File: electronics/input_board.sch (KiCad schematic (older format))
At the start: 20 parts, among them IC1 ACS713, P1 CONN_01X02, P2 CONN_02X05, P3 CONN_01X02, Q1 Q_NMOS_SGD, T1 12A

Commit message: input board -> mosfet in place of triak
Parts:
- removed T1: 12A, cyplo's:sot428, symbol THYRISTOR
- added Q?: Q_NMOS_GDSD, symbol Q_NMOS_GDSD
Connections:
- wire segments 65 -> 67
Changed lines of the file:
@@
-$EndComp
-$Comp
-L THYRISTOR T1
-U 1 1 55E0D9F8
-P 6500 2000
-F 0 "T1" V 6500 2100 50  0000 C CNN
-F 1 "12A" V 6500 1850 50  0000 C CNN
-F 2 "cyplo's:sot428" H 6500 2000 60  0001 C CNN
-F 3 "http://www.nxp.com/documents/data_sheet/BT151S_SER_L_R.pdf" H 6500 2000 60  0001 C CNN
-	1    6500 2000
-	0    -1   -1   0
 $EndComp
 $Comp
@@
 	3550 1050 3800 1050
 Wire Wire Line
-	6100 2100 6100 2300
+	6100 2000 6100 2300
 Connection ~ 6100 2100
 Wire Wire Line
@@
 Wire Wire Line
 	2850 1700 2950 1700
-Wire Wire Line
-	6500 2650 6500 2200
-Wire Wire Line
-	5750 2100 6400 2100
-Wire Wire Line
-	6500 1800 6500 1300
 $Comp
 L D_Schottky D2
@@
 Wire Wire Line
 	3350 3900 3350 3800
+Wire Wire Line
+	6200 2000 6100 2000
+Wire Wire Line
+	6100 2100 5750 2100
+Wire Wire Line
+	6500 1800 6500 1300
+Wire Wire Line
+	6500 2200 6500 2650
+$Comp
+L Q_NMOS_GDSD Q?
+U 1 1 5635FEA9
+P 6400 2000
+F 0 "Q?" H 6700 2050 50  0000 R CNN
+F 1 "Q_NMOS_GDSD" H 7100 1950 50  0000 R CNN
+F 2 "" H 6600 2100 29  0000 C CNN
+F 3 "" H 6400 2000 60  0000 C CNN
+	1    6400 2000
+	1    0    0    -1
+$EndComp
+Wire Wire Line
+	6600 1800 6500 1800
+Connection ~ 6500 1800
 $EndSCHEMATC

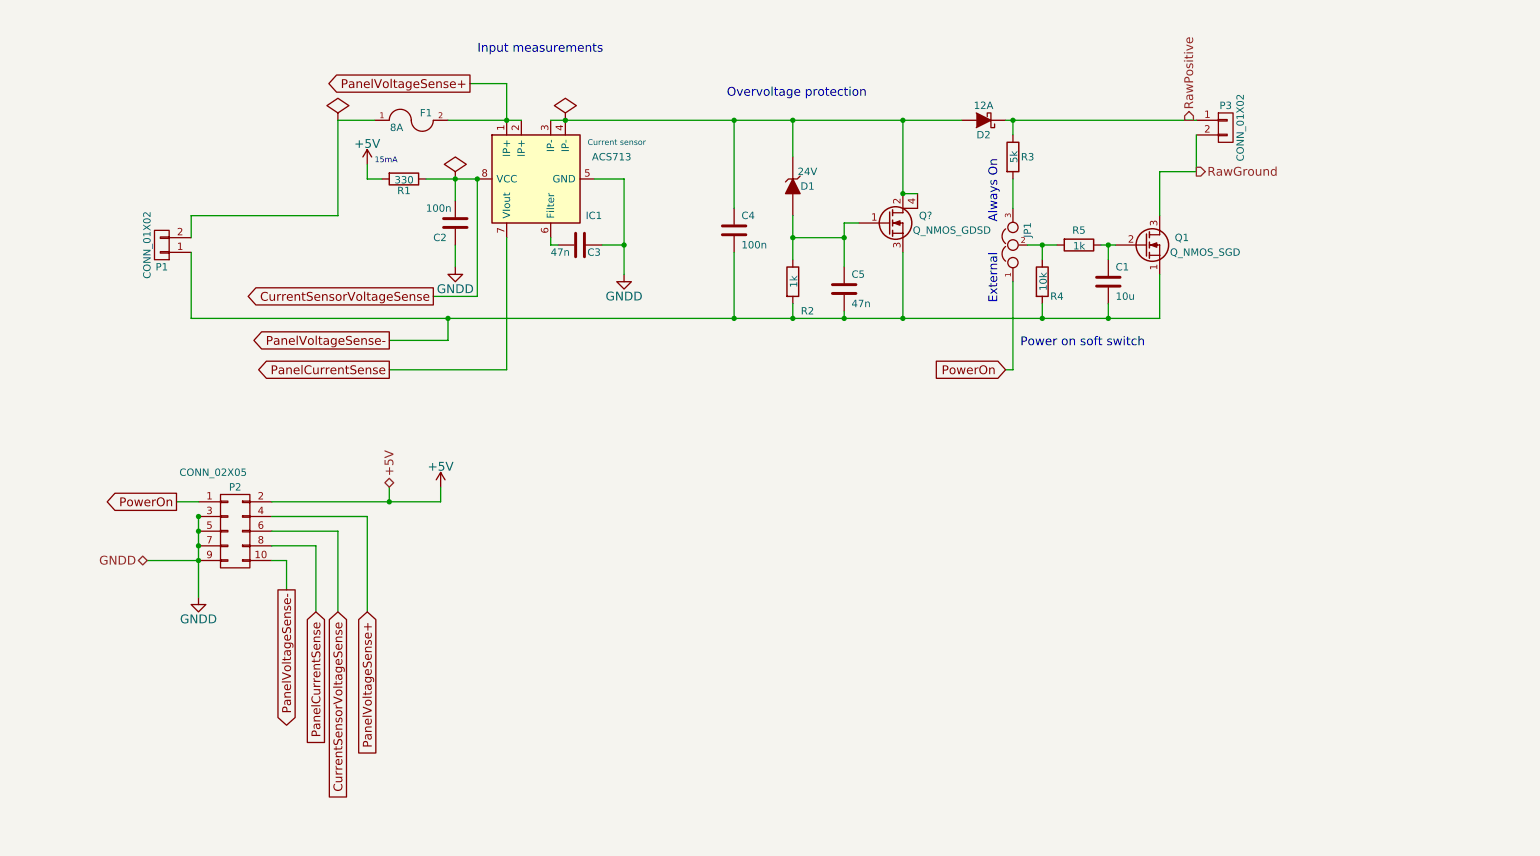
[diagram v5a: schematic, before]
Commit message: input protection: crowbar + power on switch
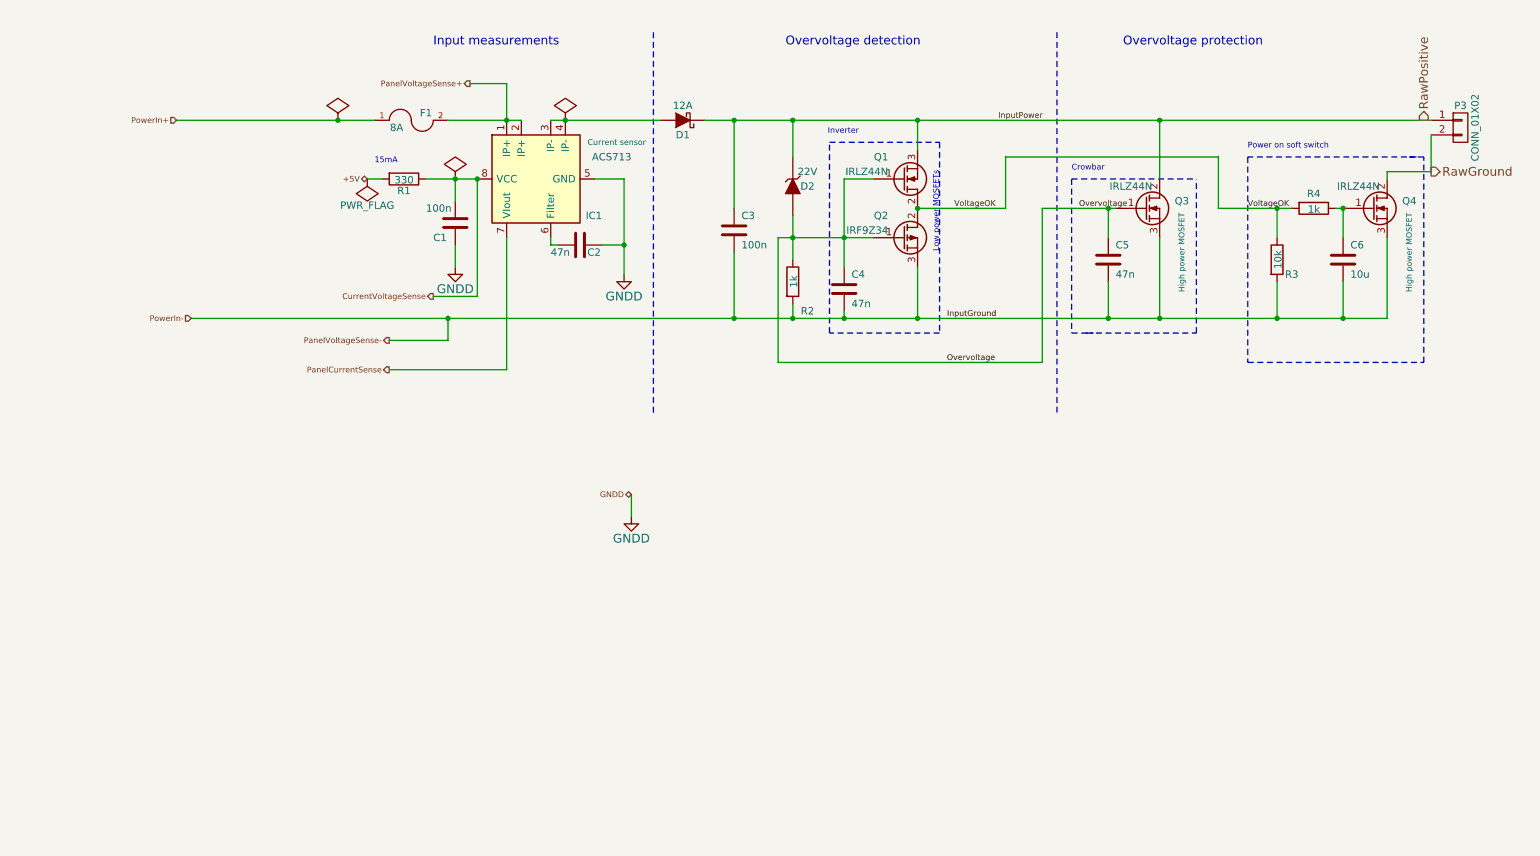
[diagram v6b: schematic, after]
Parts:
- removed JP1: JUMPER3, Pin_Headers:Pin_Header_Straight_1x03, symbol JUMPER3
- removed P1: CONN_01X02, Terminal_Blocks:TerminalBlock_WAGO-236_2Stift_RM5mm_2pol, symbol CONN_01X02
- removed P2: CONN_02X05, Pin_Headers:Pin_Header_Straight_2x05, symbol CONN_02X05
- removed Q1: Q_NMOS_SGD, cyplo's:LFPAK56, symbol Q_NMOS_SGD
- removed Q?: Q_NMOS_GDSD, symbol Q_NMOS_GDSD
- removed R3: 5k, Resistors_SMD:R_0603_HandSoldering, symbol R
- added C5: 47n, Capacitors_SMD:C_0603_HandSoldering, symbol C
- added Q1, Q3, Q4: IRLZ44N, symbol Q_NMOS_GDS
- added Q2: IRF9Z34, symbol Q_PMOS_GDS
- D2: renamed from D1; value 24V -> 22V
- renumbered C2 to C1, C3 to C2, C4 to C3, C5 to C4, C1 to C6, D2 to D1, R4 to R3, R5 to R4
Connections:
- net PanelVoltageSense-: now also C5.2, Q2.3 (S), Q3.3 (S), Q4.3 (S)
- net RawGround: now also Q4.2 (D)
- net RawPositive: now also C3.1, D2.1 (K), Q1.3 (S), Q3.2 (D)
- net at D1.2 (A), IC1.3 (IP-), IC1.4 (IP-): no longer C3.1, D2.1 (K)
- net Overvoltage: now reaches C4.1, D2.2 (A), R2.1
- net Overvoltage: now also C5.1, Q1.1 (G), Q2.1 (G), Q3.1 (G)
- net PowerIn+: now reaches F1.1
- net VoltageOK: now reaches R3.1, R4.2
- net VoltageOK: now also Q1.2 (D), Q2.2 (D)
- net at C6.1, R4.1: now also Q4.1 (G)
- net CurrentSensorVoltageSense renamed CurrentVoltageSense
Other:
- note added: "Crowbar"
- note added: "Inverter\n"
- note added: "Low power MOSFETs"
- note added: "Overvoltage detection"
- note removed: "Always On"
- note removed: "External"
- moved on the sheet: C6, D1, P3, R3, R4

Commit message: resigned from using hall effect current sensor
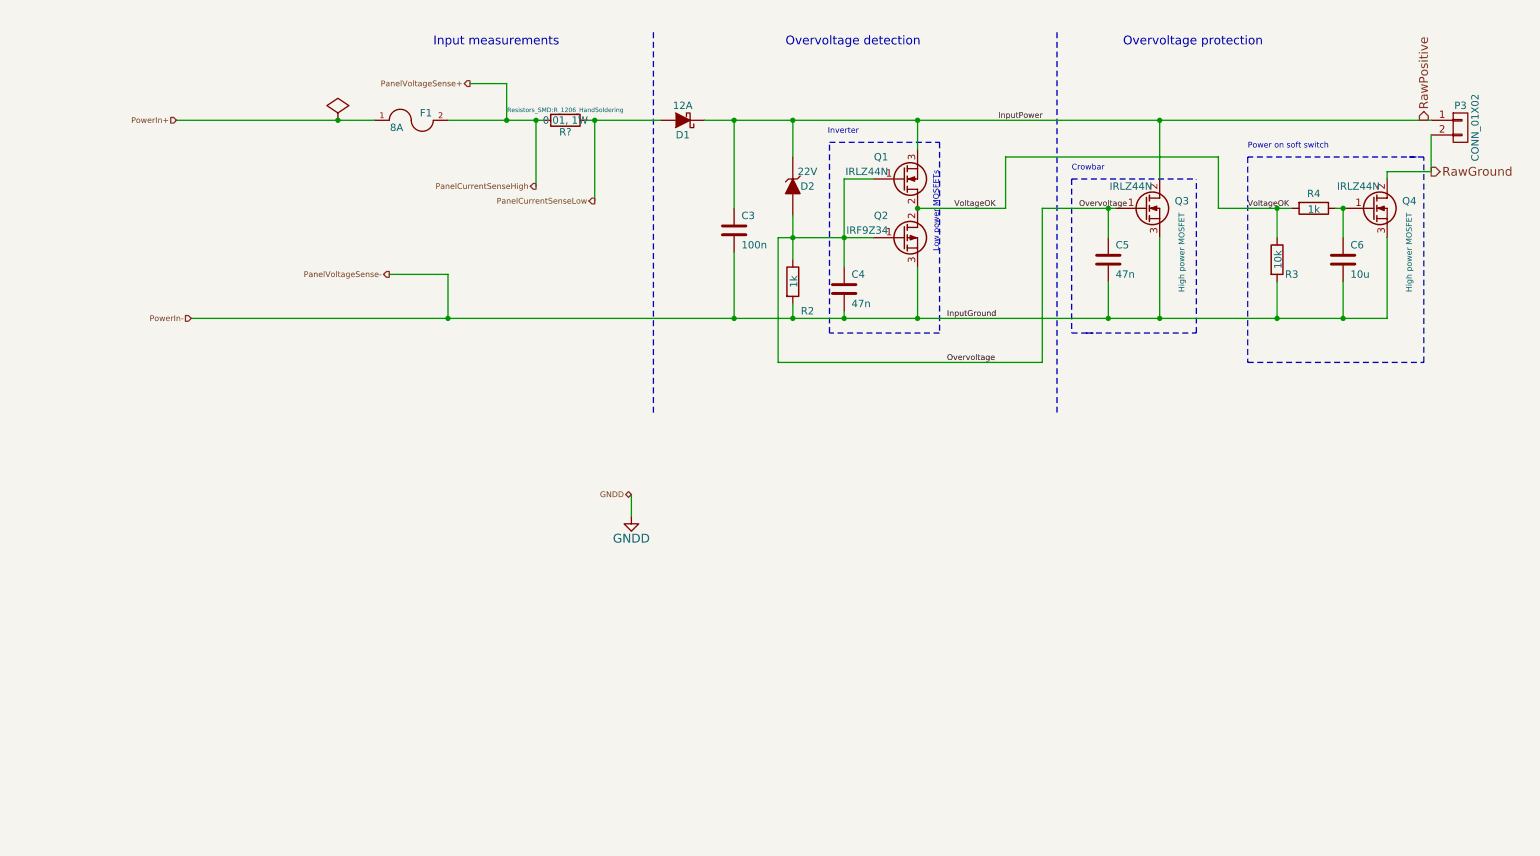
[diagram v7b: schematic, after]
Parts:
- removed C1: 100n, Capacitors_SMD:C_0603_HandSoldering, symbol C
- removed C2: 47n, Capacitors_SMD:C_0603_HandSoldering, symbol C
- removed IC1: ACS713, Housings_SOIC:SOIC-8_3.9x4.9mm_Pitch1.27mm, symbol ACS713ELCTR-30A-T
- removed R1: 330, Resistors_SMD:R_0603_HandSoldering, symbol R
- added R?: 0.01, 1W, Resistors_SMD:R_1206_HandSoldering, symbol R
- D1: footprint cyplo's:TO277A -> Diodes_SMD:D-Pak_TO252AA
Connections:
- net PanelCurrentSenseLow: now reaches D1.2 (A)
- net PanelCurrentSenseLow: now also R?.1
- net PanelVoltageSense+ renamed PanelCurrentSenseHigh
- net PanelCurrentSenseHigh: now also R?.2
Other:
- note removed: "15mA"
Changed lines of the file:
@@
 	0    1    1    0
-$EndComp
-$Comp
-L C C1
-U 1 1 55E0DA1B
-P 3450 2000
-F 0 "C1" H 3300 1900 50  0000 L CNN
-F 1 "100n" H 3250 2100 50  0000 L CNN
-F 2 "Capacitors_SMD:C_0603_HandSoldering" H 3488 1850 30  0001 C CNN
-F 3 "" H 3450 2000 60  0000 C CNN
-	1    3450 2000
-	1    0    0    -1
-$EndComp
-$Comp
-L C C2
-U 1 1 55E0DA22
-P 4300 2150
-F 0 "C2" V 4350 2200 50  0000 L CNN
-F 1 "47n" V 4350 1950 50  0000 L CNN
-F 2 "Capacitors_SMD:C_0603_HandSoldering" H 4338 2000 30  0001 C CNN
-F 3 "" H 4300 2150 60  0000 C CNN
-	1    4300 2150
-	0    1    1    0
-$EndComp
-$Comp
-L R R1
-U 1 1 55E0DA2C
-P 3100 1700
-F 0 "R1" V 3180 1700 50  0000 C CNN
-F 1 "330" V 3107 1701 50  0000 C CNN
-F 2 "Resistors_SMD:R_0603_HandSoldering" V 3030 1700 30  0001 C CNN
-F 3 "" H 3100 1700 30  0000 C CNN
-	1    3100 1700
-	0    1    1    0
-$EndComp
-$Comp
-L ACS713ELCTR-30A-T IC1
-U 1 1 55E0DA34
-P 4000 1700
-F 0 "IC1" V 4250 1250 50  0000 L CNN
-F 1 "ACS713" V 3850 1050 50  0000 L CNN
-F 2 "Housings_SOIC:SOIC-8_3.9x4.9mm_Pitch1.27mm" H 4000 1700 50  0001 C CIN
-F 3 "http://www.allegromicro.com/en/Products/Part_Numbers/0713/0713.pdf" H 4100 2150 60  0001 C CNN
-F 4 "Current sensor" V 3750 1150 39  0000 C CNN "Note"
-	1    4000 1700
-	0    -1   1    0
 $EndComp
 Text Notes 5700 800  0    60   ~ 0
@@
 Text Notes 8850 1500 0    39   ~ 0
 Power on soft switch
-$Comp
-L GNDD #PWR06
-U 1 1 55E0DA4C
-P 3450 2300
-F 0 "#PWR06" H 3450 2050 60  0001 C CNN
-F 1 "GNDD" H 3450 2150 60  0000 C CNN
-F 2 "" H 3450 2300 60  0000 C CNN
-F 3 "" H 3450 2300 60  0000 C CNN
-	1    3450 2300
-	1    0    0    -1
-$EndComp
-$Comp
-L GNDD #PWR07
-U 1 1 55E0DA5C
-P 4600 2350
-F 0 "#PWR07" H 4600 2100 60  0001 C CNN
-F 1 "GNDD" H 4600 2200 60  0000 C CNN
-F 2 "" H 4600 2350 60  0000 C CNN
-F 3 "" H 4600 2350 60  0000 C CNN
-	1    4600 2350
-	1    0    0    -1
-$EndComp
 $Comp
 L CONN_01X02 P3
@@
 	1    0    0    -1
 $EndComp
-$Comp
-L PWR_FLAG #FLG08
-U 1 1 55E0DA69
-P 4200 1300
-F 0 "#FLG08" H 4200 1395 30  0001 C CNN
-F 1 "PWR_FLAG" H 4200 1480 30  0001 C CNN
-F 2 "" H 4200 1300 60  0000 C CNN
-F 3 "" H 4200 1300 60  0000 C CNN
-	1    4200 1300
-	1    0    0    -1
-$EndComp
 Connection ~ 5750 1300
 Connection ~ 5750 2650
@@
 Wire Wire Line
 	9800 1650 10100 1650
-Connection ~ 4200 1300
-Wire Wire Line
-	3400 1300 3900 1300
-Wire Wire Line
-	1550 1300 2900 1300
+Wire Wire Line
+	3400 1300 3800 1300
+Wire Wire Line
+	3800 1300 4000 1300
+Wire Wire Line
+	4000 1300 4050 1300
+Wire Wire Line
+	1550 1300 2650 1300
+Wire Wire Line
+	2650 1300 2900 1300
 Wire Wire Line
 	3800 1050 3800 1300
@@
 	5750 1300 5750 1550
 Wire Wire Line
-	5750 1950 5750 2250
+	5750 1950 5750 2100
+Wire Wire Line
+	5750 2100 5750 2250
 Connection ~ 5750 2100
 Connection ~ 9050 2650
 Connection ~ 9050 1900
 Wire Wire Line
-	3800 3000 3000 3000
-Wire Wire Line
 	3550 1050 3800 1050
 Connection ~ 6100 2100
@@
 	9800 2650 9800 2100
 Wire Wire Line
-	5150 1300 10100 1300
-Wire Wire Line
-	3400 2800 3400 2650
+	5150 1300 5350 1300
+Wire Wire Line
+	5350 1300 5750 1300
+Wire Wire Line
+	5750 1300 6600 1300
+Wire Wire Line
+	6600 1300 8250 1300
+Wire Wire Line
+	8250 1300 10100 1300
+Wire Wire Line
+	3400 2350 3400 2650
 Connection ~ 3400 2650
 Wire Wire Line
-	3400 2800 3000 2800
-Wire Wire Line
-	4100 2100 4100 2150
-Wire Wire Line
-	4600 1700 4600 2350
-Wire Wire Line
-	4450 2150 4600 2150
-Connection ~ 4600 2150
+	3400 2350 3000 2350
 Wire Wire Line
 	10100 1650 10100 1400
-Wire Wire Line
-	4600 1700 4400 1700
-Wire Wire Line
-	3250 1700 3600 1700
-Wire Wire Line
-	3450 2150 3450 2300
-Wire Wire Line
-	3450 1700 3450 1850
-Connection ~ 3450 1700
-Wire Wire Line
-	2850 1700 2950 1700
 $Comp
 L PWR_FLAG #FLG09
@@
 	1    0    0    -1
 $EndComp
-Text Notes 2900 1600 0    39   ~ 0
-15mA
-$Comp
-L PWR_FLAG #FLG010
-U 1 1 55E0DAB3
-P 3450 1700
-F 0 "#FLG010" H 3450 1795 30  0001 C CNN
-F 1 "PWR_FLAG" H 3450 1880 30  0001 C CNN
-F 2 "" H 3450 1700 60  0000 C CNN
-F 3 "" H 3450 1700 60  0000 C CNN
-	1    3450 1700
-	1    0    0    -1
-$EndComp
-Wire Wire Line
-	3600 1700 3600 2500
-Wire Wire Line
-	3600 2500 3300 2500
-Connection ~ 3600 1700
 Wire Wire Line
 	9450 1900 9500 1900
@@
 Wire Wire Line
 	5750 2650 5750 2550
-Wire Wire Line
-	4100 2150 4150 2150
 $Comp
 L D_Schottky D1
@@
 F 0 "D1" H 5000 1400 50  0000 C CNN
 F 1 "12A" H 5000 1200 50  0000 C CNN
-F 2 "cyplo's:TO277A" H 5000 1300 60  0001 C CNN
+F 2 "Diodes_SMD:D-Pak_TO252AA" H 5000 1300 60  0001 C CNN
 F 3 "http://www.vishay.com/docs/89094/v12p12.pdf" H 5000 1300 60  0001 C CNN
 	1    5000 1300
@@
 RawGround
 Wire Wire Line
-	5650 2100 6300 2100
+	5650 2100 5750 2100
+Wire Wire Line
+	5750 2100 6100 2100
+Wire Wire Line
+	6100 2100 6300 2100
 $Comp
 L Q_NMOS_GDS Q4
@@
 $EndComp
 Wire Wire Line
-	6100 1700 6100 2300
+	6100 1700 6100 2100
+Wire Wire Line
+	6100 2100 6100 2300
 Wire Wire Line
 	6100 1700 6300 1700
@@
 Overvoltage
 Wire Wire Line
-	4100 1300 4850 1300
-Wire Wire Line
-	1650 2650 9800 2650
-Wire Wire Line
-	8650 1900 9150 1900
+	4350 1300 4400 1300
+Wire Wire Line
+	4400 1300 4850 1300
+Wire Wire Line
+	1650 2650 3400 2650
+Wire Wire Line
+	3400 2650 5350 2650
+Wire Wire Line
+	5350 2650 5750 2650
+Wire Wire Line
+	5750 2650 6100 2650
+Wire Wire Line
+	6100 2650 6600 2650
+Wire Wire Line
+	6600 2650 7900 2650
+Wire Wire Line
+	7900 2650 8250 2650
+Wire Wire Line
+	8250 2650 9050 2650
+Wire Wire Line
+	9050 2650 9500 2650
+Wire Wire Line
+	9500 2650 9800 2650
+Wire Wire Line
+	8650 1900 9050 1900
+Wire Wire Line
+	9050 1900 9150 1900
 Text Label 8850 1900 0    39   ~ 0
 VoltageOK
@@
 InputPower
 Wire Wire Line
-	7450 1900 7950 1900
+	7450 1900 7900 1900
+Wire Wire Line
+	7900 1900 7950 1900
 Text Label 7700 1900 0    39   ~ 0
 Overvoltage
@@
 Text Notes 7650 1650 0    39   ~ 0
 Crowbar
-Text HLabel 2850 1700 0    39   BiDi ~ 0
-+5V
-Text HLabel 3000 3000 0    39   Output ~ 0
-PanelCurrentSense
+Text HLabel 4000 1750 0    39   Output ~ 0
+PanelCurrentSenseHigh
 Text HLabel 4650 3850 0    39   BiDi ~ 0
 GNDD
@@
 Wire Wire Line
 	4650 3850 4650 4000
-Text HLabel 3000 2800 0    39   Output ~ 0
+Text HLabel 3000 2350 0    39   Output ~ 0
 PanelVoltageSense-
 Text HLabel 3550 1050 0    39   Output ~ 0
 PanelVoltageSense+
-Text HLabel 3300 2500 0    39   Output ~ 0
-CurrentVoltageSense
-$Comp
-L PWR_FLAG #FLG012
-U 1 1 566DC42F
-P 2850 1700
-F 0 "#FLG012" H 2850 1795 50  0001 C CNN
-F 1 "PWR_FLAG" H 2850 1880 50  0000 C CNN
-F 2 "" H 2850 1700 60  0000 C CNN
-F 3 "" H 2850 1700 60  0000 C CNN
-	1    2850 1700
-	-1   0    0    1
-$EndComp
-Wire Wire Line
-	3800 2100 3800 3000
 Text HLabel 1650 2650 0    39   Input ~ 0
 PowerIn-
@@
 Text HLabel 1550 1300 0    39   Input ~ 0
 PowerIn+
+$Comp
+L R R?
+U 1 1 56756EEE
+P 4200 1300
+F 0 "R?" V 4280 1300 50  0000 C CNN
+F 1 "0.01, 1W" V 4200 1300 50  0000 C CNN
+F 2 "Resistors_SMD:R_1206_HandSoldering" V 4130 1300 30  0000 C CNN
+F 3 "" H 4200 1300 30  0000 C CNN
+	1    4200 1300
+	0    1    1    0
+$EndComp
+Wire Wire Line
+	4000 1300 4000 1750
+Connection ~ 4000 1300
+Wire Wire Line
+	4400 1300 4400 1850
+Connection ~ 4400 1300
+Text HLabel 4400 1850 0    39   Output ~ 0
+PanelCurrentSenseLow
 $EndSCHEMATC
